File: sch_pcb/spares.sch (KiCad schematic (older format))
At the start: 77 parts, among them J301 SPARE, J302 SPARE, J303 SPARE, J304 SPARE, J305 USER_GPIO, J306 SPARE, J307 SPARE, J308 SPARE, J309 SPARE, J310 SPARE, J311 SPARE, J312 USER_ADC, J313 SPARE, J314 SPARE, J315 12VDC_IN, Q301 SPARE, Q302 SPARE, U106 MCP4351, U301 MCP23017, U302 SPARE, U303 SPARE, U304 MCP3008, U305 MCP1703A-2502/MB, U306 TPS54302

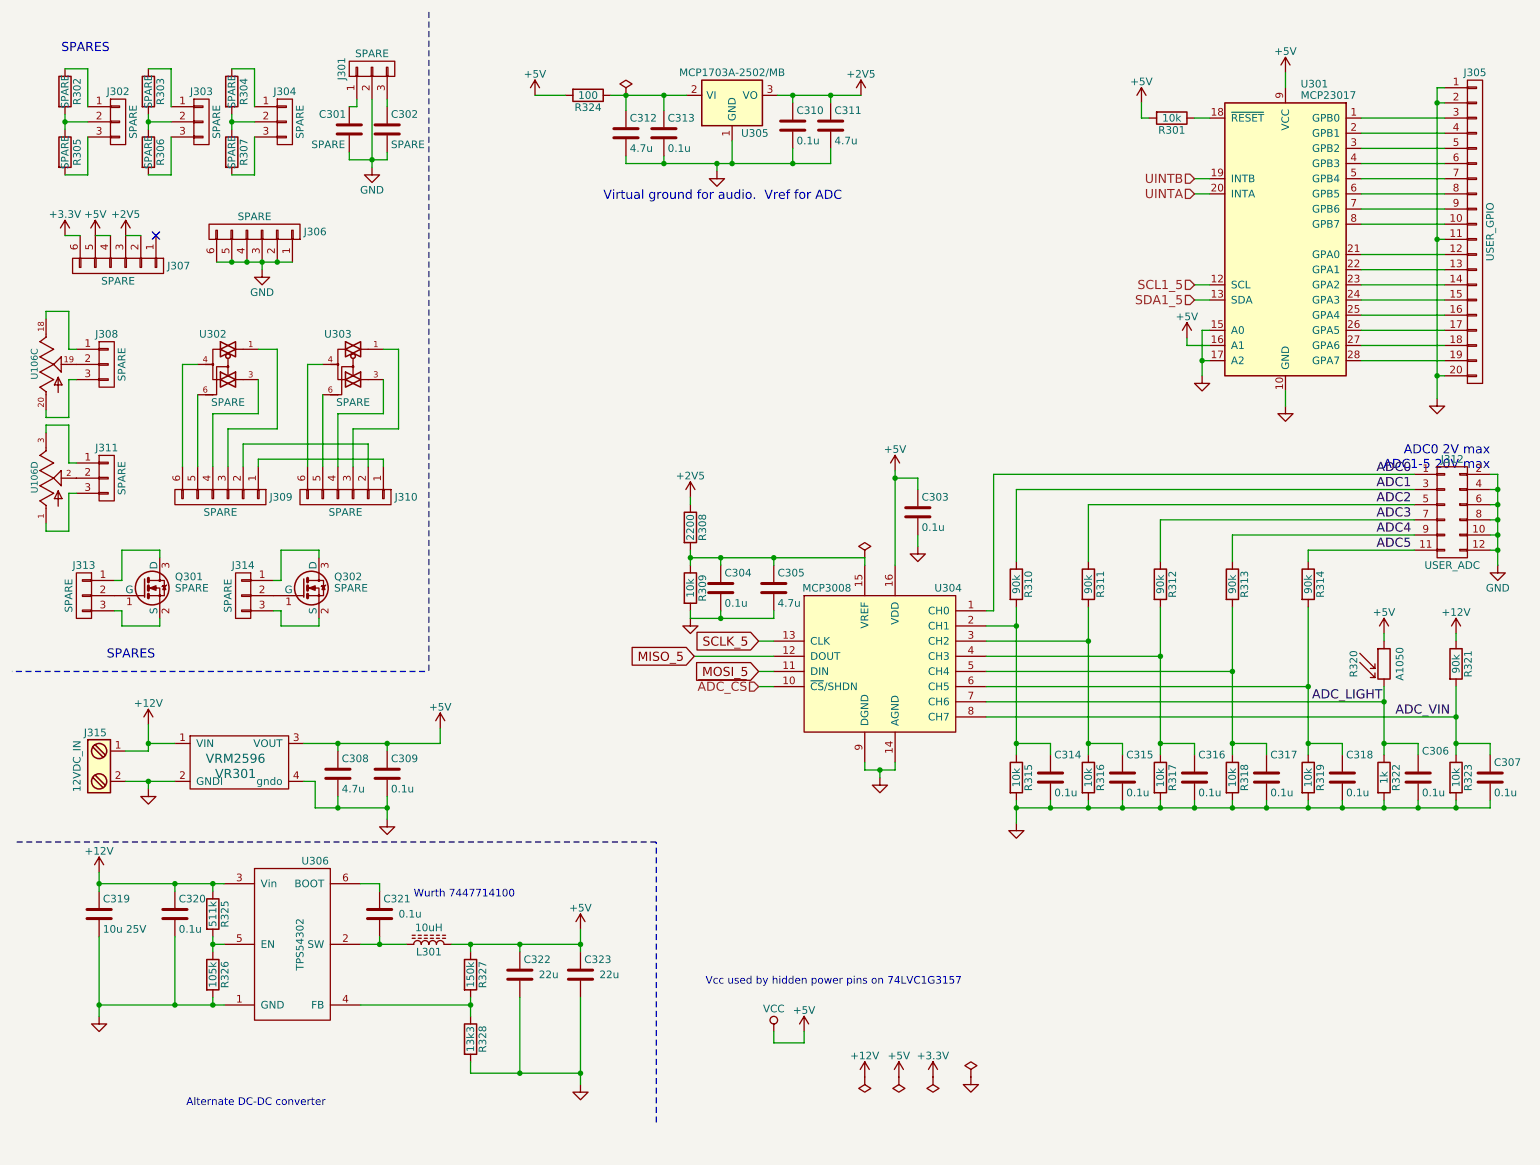
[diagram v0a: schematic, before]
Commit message: Updates based on emails
Disconnect SDO on PGAs
Add mounting holes 
More placement on PCB - for now, delete all 4xx sheet footprints.  Once channel 1 is placed, it will get copied to make channel 2.
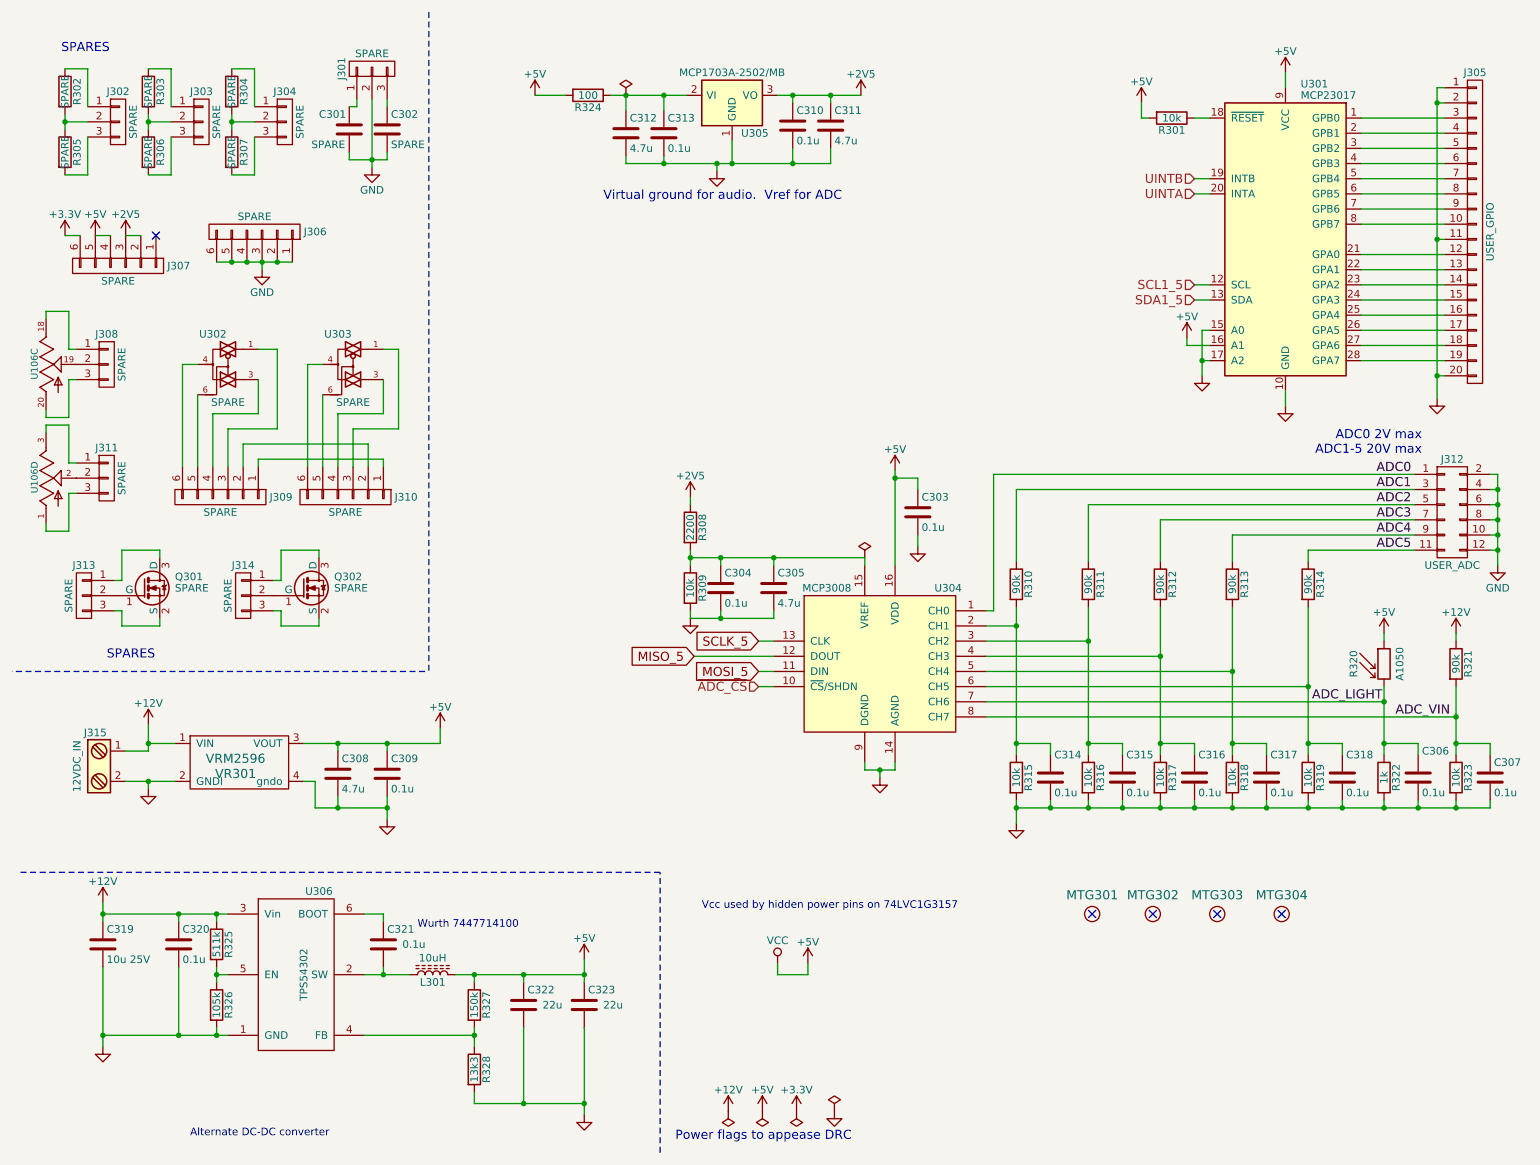
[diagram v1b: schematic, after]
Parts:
- added MTG301, MTG302, MTG303, MTG304: MOUNTING_HOLE, lib:MTG_4_40, symbol MOUNTING_HOLE
- C311, C312, C313, C314, C315, C316, C317, C318: footprint lib:smd0805 -> lib:smd0603
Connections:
- no-connect marks 1 -> 5
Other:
- note added: "Power flags to appease DRC"
- moved on the sheet: C319, C320, C321, C322, C323, L301, R325, R326, R327, R328, U306

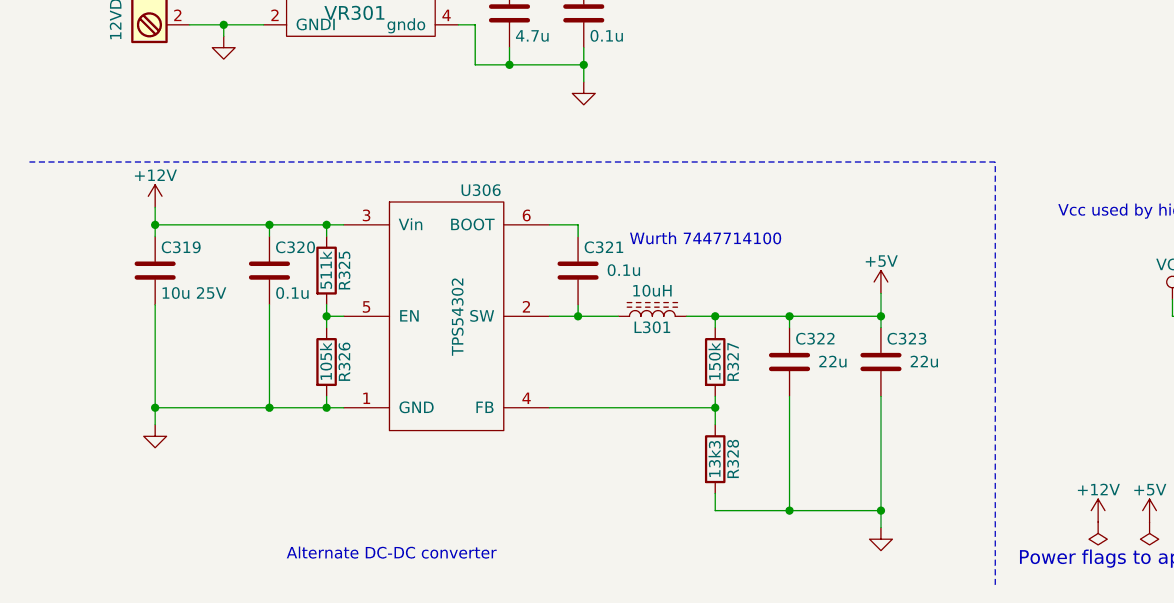
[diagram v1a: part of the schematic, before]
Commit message: Add files via upload
Fix missing pin numbers on opamps
Change two 4.7uF caps in parallel to 10uF/0805.  This will save 6 caps and will handle capacitance loss due to DC bias better
Change 2 22uF caps to 4 10uF caps to get rid of an extra BOM line item
More work on placement.  The channel now fits in the space allocated to it. 
Connectors need to be revisited - GPIO and soundcard
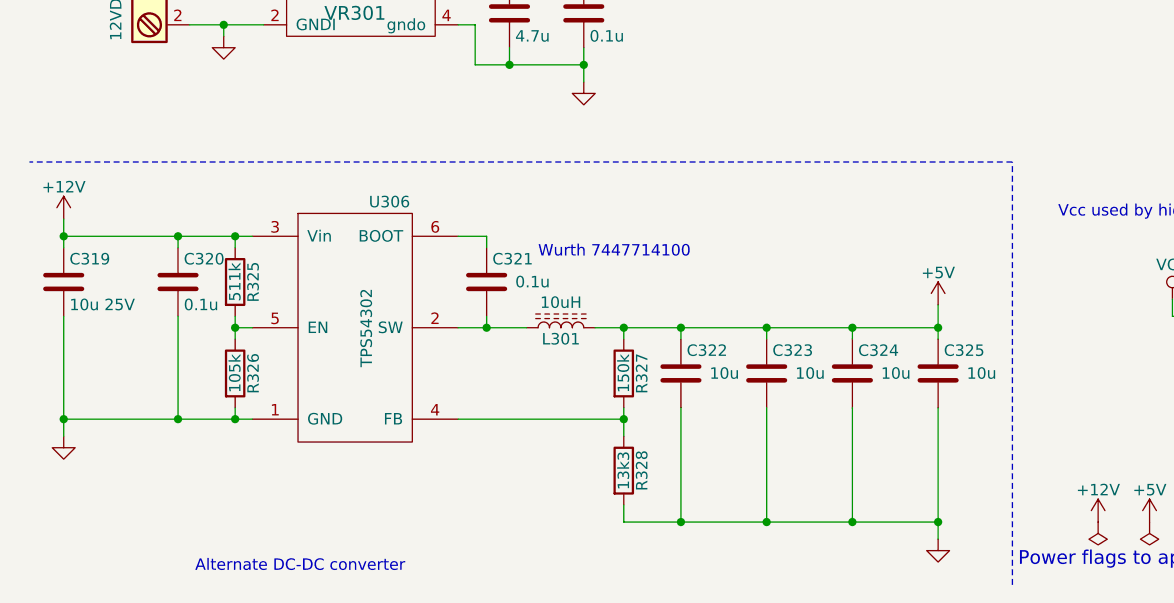
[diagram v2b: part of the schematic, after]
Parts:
- added C324, C325: 10u, lib:smd0805, symbol C
- C322, C323: value 22u -> 10u
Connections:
- net +5V: now also C324.1, C325.1
- net GND: now also C324.2, C325.2
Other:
- moved on the sheet: C319, C320, C321, C322, C323, L301, R325, R326, R327, R328, U306

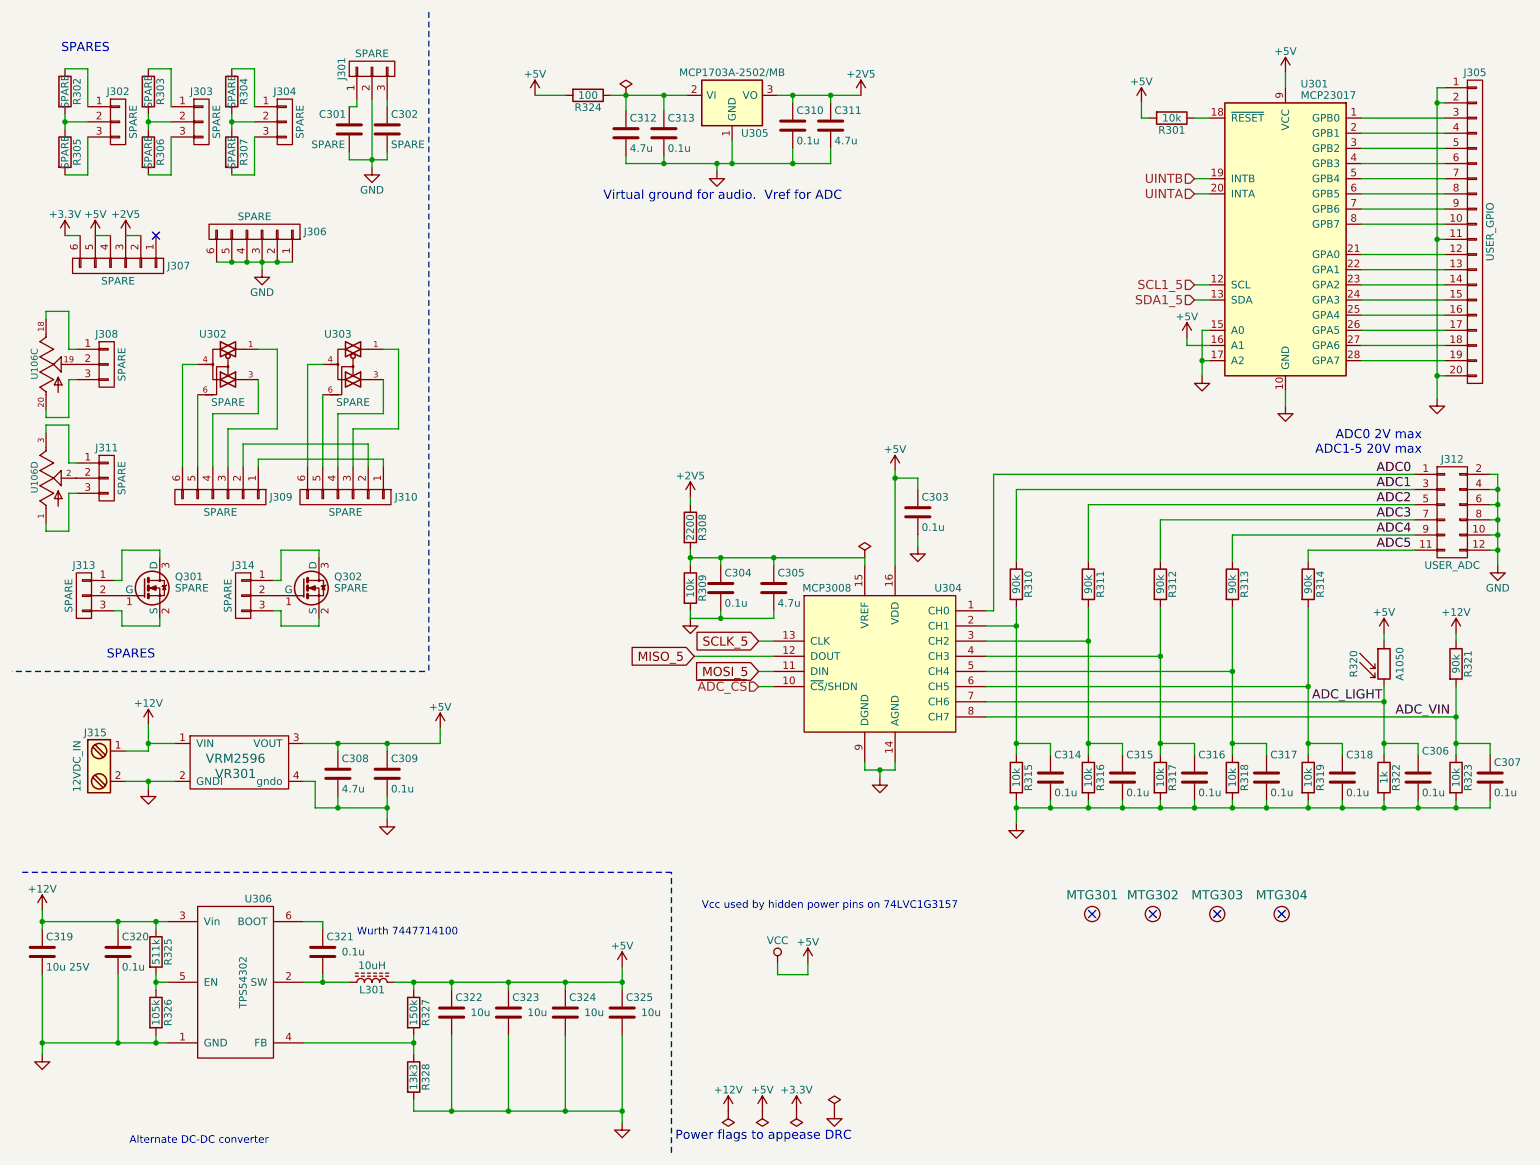
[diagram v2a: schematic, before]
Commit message: Add files via upload
Changed  user_adc connector to 2x7 (14-pin is a lot more common than 12-pin)
Changed user_gpio connector to 2 2x8 connectors.  1x20 takes too much linear space
First pass layout on the two audio channels.  Right now, board is 4-layer, 100x150mm.  May be able to knock down the 150mm dimension 
The link and soundcard connectors fit in a row across the front edge.
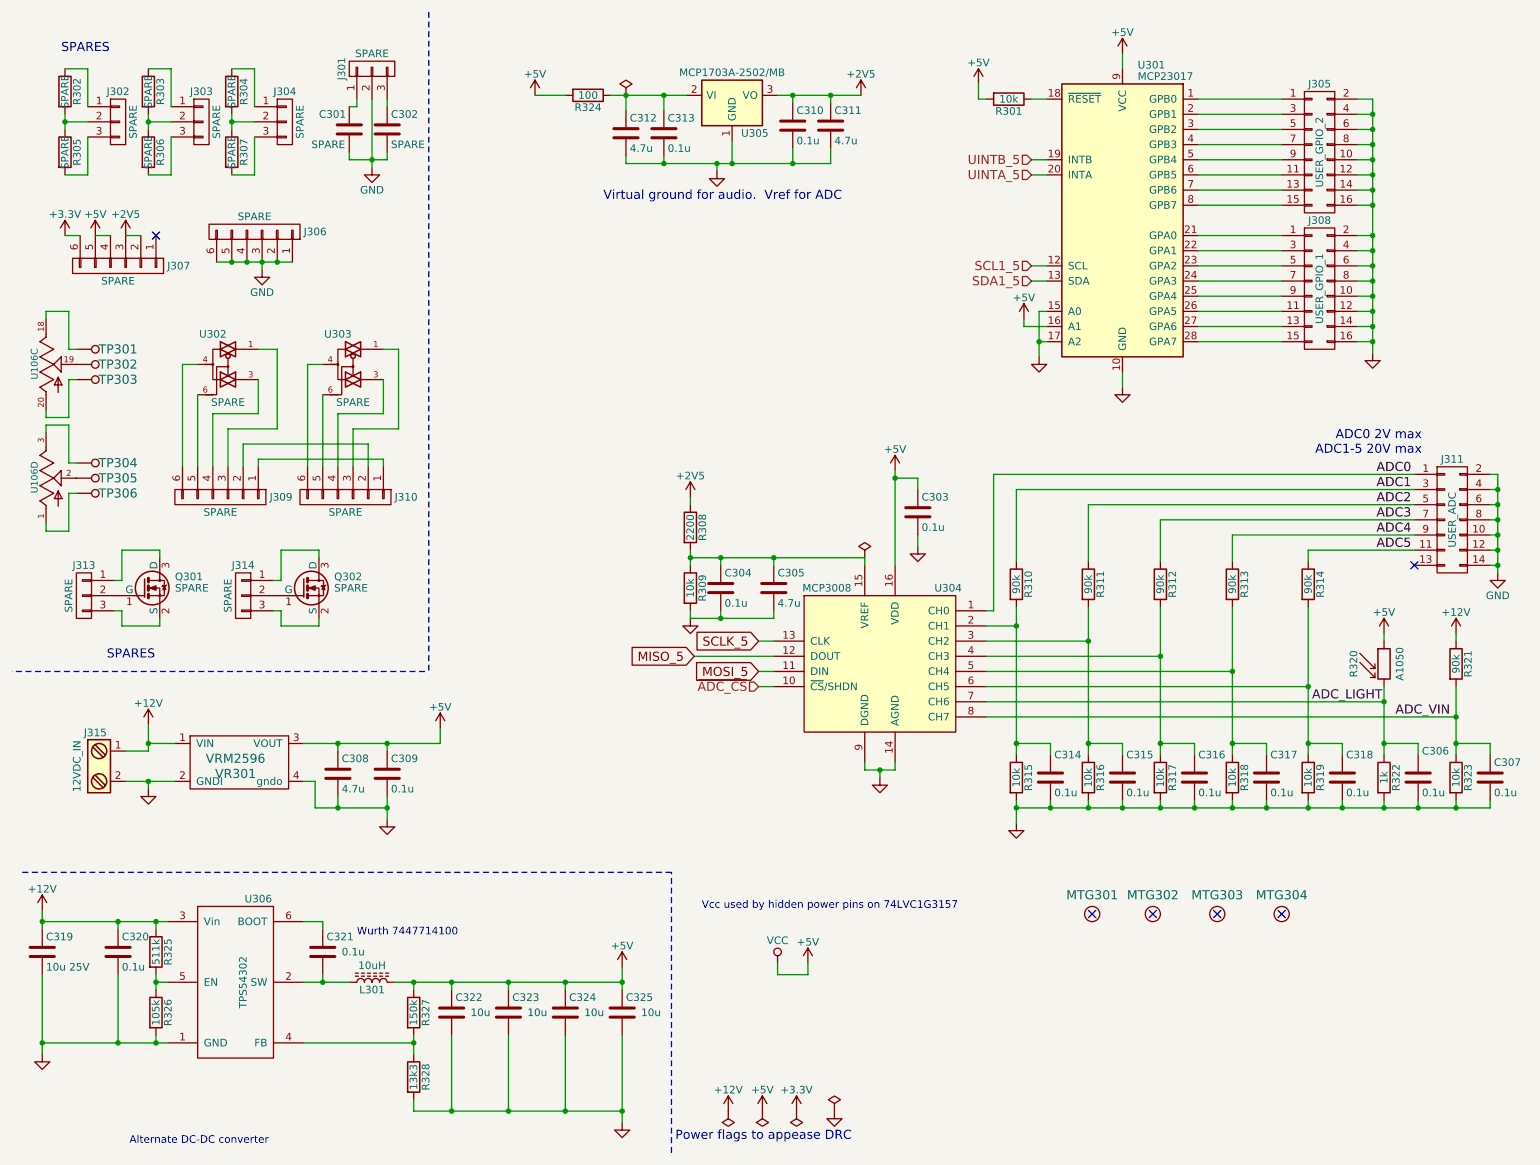
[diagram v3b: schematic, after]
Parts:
- removed J305: USER_GPIO, lib:SIL-20, symbol CONN_01X20
- removed J308, J311: SPARE, lib:SIL-3, symbol CONN_01X03
- removed J312: USER_ADC, lib:pin_array_6x2, symbol CONN_02X06
- added J305: USER_GPIO_2, lib:RibbonHeader2x8, symbol CONN_02X08
- added J308: USER_GPIO_1, lib:RibbonHeader2x8, symbol CONN_02X08
- added J311: USER_ADC, lib:RibbonHeader2x7, symbol CONN_02X07
- added TP301, TP302, TP303, TP304, TP305, TP306: TESTPOINT, lib:Wire_28AWG, symbol TESTPOINT
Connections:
- net ADC0: now also J311.1 (P1)
- net ADC1: now also J311.3 (P3)
- net ADC2: now also J311.5 (P5)
- net ADC3: now also J311.7 (P7)
- net ADC4: now also J311.9 (P9)
- net ADC5: now also J311.11 (P11)
- net GND: now also J305.10 (P10), J305.12 (P12), J305.14 (P14), J305.16 (P16), J305.2 (P2), J305.4 (P4), J305.6 (P6), J305.8 (P8), J308.10 (P10), J308.12 (P12), J308.14 (P14), J308.16 (P16), J308.2 (P2), J308.4 (P4), J308.6 (P6), J308.8 (P8), J311.10 (P10), J311.12 (P12), J311.14 (P14), J311.2 (P2), J311.4 (P4), J311.6 (P6), J311.8 (P8)
- net at U106.1 (A): now also TP306.1
- net at U106.2 (W): now also TP305.1
- net at U106.3 (B): now also TP304.1
- net at U106.18 (B): now also TP301.1
- net at U106.19 (W): now also TP302.1
- net at U106.20 (A): now also TP303.1
- net at U301.1 (GPB0): now also J305.1 (P1)
- net at U301.2 (GPB1): now also J305.3 (P3)
- net at U301.21 (GPA0): now also J308.1 (P1)
- net at U301.22 (GPA1): now also J308.3 (P3)
- net at U301.23 (GPA2): now also J308.5 (P5)
- net at U301.24 (GPA3): now also J308.7 (P7)
- net at U301.25 (GPA4): now also J308.9 (P9)
- net at U301.26 (GPA5): now also J308.11 (P11)
- net at U301.27 (GPA6): now also J308.13 (P13)
- net at U301.28 (GPA7): now also J308.15 (P15)
- net at U301.3 (GPB2): now also J305.5 (P5)
- net at U301.4 (GPB3): now also J305.7 (P7)
- net at U301.5 (GPB4): now also J305.9 (P9)
- net at U301.6 (GPB5): now also J305.11 (P11)
- net at U301.7 (GPB6): now also J305.13 (P13)
- net at U301.8 (GPB7): now also J305.15 (P15)
- net UINTA renamed UINTA_5
- net UINTB renamed UINTB_5
- no-connect marks 5 -> 6
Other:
- moved on the sheet: R301, U301
